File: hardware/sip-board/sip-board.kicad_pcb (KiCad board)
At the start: 8 copper layers, 43 parts, among them IC1 XC7S15-1CPGA196C, J1 Conn_01x06_Pin, J2 Conn_01x10_Pin, J3 Conn_01x10_Pin, J4 Conn_01x10_Pin, J5 Conn_01x10_Pin, SW1 SW_DIP_x03, U1 M95256-WMN6P, U2 TLV75710PDRV, U3 TLV75718PDRV, U4 TLV75733PDRV

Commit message: begin layout for sip
we will need to use pcbway
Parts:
- added C10: 0.47u, Capacitor_SMD:C_0201_0603Metric, F.Cu at (18.9, 62.8)
- added C11: 0.47u, Capacitor_SMD:C_0201_0603Metric, F.Cu at (18.9, 64.6)
- added C12: 47u, Capacitor_SMD:C_0201_0603Metric, F.Cu at (18.9, 66.3)
- added C13: 4.7u, Capacitor_SMD:C_0201_0603Metric, F.Cu at (18.9, 68.1)
- added C14: 0.47u, Capacitor_SMD:C_0201_0603Metric, F.Cu at (21.3, 57.6)
- added C15: 47u, Capacitor_SMD:C_0201_0603Metric, F.Cu at (21.3, 59.3)
- added C16: 4.7u, Capacitor_SMD:C_0201_0603Metric, F.Cu at (21.3, 61.1)
- added C17: 0.47u, Capacitor_SMD:C_0201_0603Metric, F.Cu at (21.3, 62.8)
- added C18: 0.47u, Capacitor_SMD:C_0201_0603Metric, F.Cu at (21.3, 64.6)
- added C19: 0.47u, Capacitor_SMD:C_0201_0603Metric, F.Cu at (21.3, 66.3)
- added C20: 0.47u, Capacitor_SMD:C_0201_0603Metric, F.Cu at (21.3, 68.1)
- added C21: 100u, Capacitor_SMD:C_0201_0603Metric, F.Cu at (23.8, 57.6)
- added C22: 4.7u, Capacitor_SMD:C_0201_0603Metric, F.Cu at (23.8, 59.3)
- added C23: 4.7u, Capacitor_SMD:C_0201_0603Metric, F.Cu at (23.8, 61.1)
- added C24: 0.47u, Capacitor_SMD:C_0201_0603Metric, F.Cu at (23.8, 62.8)
- added C25: 0.47u, Capacitor_SMD:C_0201_0603Metric, F.Cu at (23.8, 64.6)
- added C26: 0.47u, Capacitor_SMD:C_0201_0603Metric, F.Cu at (23.8, 66.3)
- added C27: 0.47u, Capacitor_SMD:C_0201_0603Metric, F.Cu at (23.8, 68.1)
- added C28: 0.47u, Capacitor_SMD:C_0201_0603Metric, F.Cu at (26.2, 57.6)
- added C29: 0.47u, Capacitor_SMD:C_0201_0603Metric, F.Cu at (26.2, 59.3)
- added C30: 100u, Capacitor_SMD:C_0201_0603Metric, F.Cu at (26.2, 61.1)
- added C31: 4.7u, Capacitor_SMD:C_0201_0603Metric, F.Cu at (26.2, 62.8)
- added C32: 4.7u, Capacitor_SMD:C_0201_0603Metric, F.Cu at (26.2, 64.6)
- added C33: 0.47u, Capacitor_SMD:C_0201_0603Metric, F.Cu at (26.2, 66.3)
- added C34: 0.47u, Capacitor_SMD:C_0201_0603Metric, F.Cu at (26.2, 68.1)
- added C35: 0.47u, Capacitor_SMD:C_0201_0603Metric, F.Cu at (28.7, 57.6)
- added C36: 0.47u, Capacitor_SMD:C_0201_0603Metric, F.Cu at (28.7, 59.3)
- added C37: 100u, Capacitor_SMD:C_0201_0603Metric, F.Cu at (28.7, 61.1)
- added C38: 4.7u, Capacitor_SMD:C_0201_0603Metric, F.Cu at (28.7, 62.8)
- added C39: 4.7u, Capacitor_SMD:C_0201_0603Metric, F.Cu at (28.7, 64.6)
- added C7: 100u, Capacitor_SMD:C_0201_0603Metric, F.Cu at (18.9, 57.6)
- added C8: 4.7u, Capacitor_SMD:C_0201_0603Metric, F.Cu at (18.9, 59.3)
- added C9: 4.7u, Capacitor_SMD:C_0201_0603Metric, F.Cu at (18.9, 61.1)
- moved IC1 102.8 mm to (148.9, 90.1)
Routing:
- net +3.3V: track 0.00 -> 15.4 mm, vias 0 -> 11
- net +1V0: track 0.00 -> 11.6 mm, vias 0 -> 11
- net +1V8: track 0.00 -> 4.97 mm, vias 0 -> 4
- net GND: track 0.00 -> 0.71 mm
- added copper zone on F.Cu, net GND
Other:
- board outline added: 20.5 x 21.7 mm
- board text added: "PCBway can do smallest 0.15mm annular width for buried/blind vias"

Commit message: fix some connections, layout
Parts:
- removed J1: Conn_01x06_Pin, Connector_PinHeader_2.54mm:PinHeader_1x06_P2.54mm_Vertical
- removed J2, J3, J4, J5: Conn_01x10_Pin, Connector_PinHeader_2.54mm:PinHeader_1x10_P2.54mm_Vertical
- added C40: 10u, Capacitor_SMD:C_0201_0603Metric, F.Cu at (142.7, 117.9)
- added JTAG: Conn_01x06_Pin, Connector_PinHeader_2.54mm:PinHeader_1x06_P2.54mm_Vertical_SMD_Pin1Right, F.Cu at (146.8, 89.7)
- added R16: 5k, Resistor_SMD:R_0201_0603Metric, F.Cu at (152.7, 110.4)
- added SW2: SW_RESET, Button_Switch_SMD:SW_Push_1P1T_NO_6x6mm_H9.5mm, F.Cu at (147.2, 113.7)
- C10, C11, C16, C17, C18, C19, C20, C21, C22, C23, C24, C25, C26, C27, C28, C29, C30, C31, C32, C33, C34, C35, C36, C37, C38, C39, C7, C8, C9, U1, U5, U6: moved to B.Cu
- moved U5 140.8 mm to (142.5, 93.0), turned to 180 degrees
- moved U6 139.4 mm to (142.5, 96.1), turned to 180 degrees
- moved C7 135.3 mm to (145.8, 104.2), turned to 180 degrees
- moved C8 135.0 mm to (145.8, 105.0), turned to 180 degrees
- moved C10 134.8 mm to (147.0, 104.6), turned to -90 degrees
- moved C11 134.7 mm to (147.0, 106.1), turned to 90 degrees
- moved C9 134.6 mm to (145.8, 105.8), turned to 180 degrees
- moved C15 134.4 mm to (153.8, 81.8), turned to -90 degrees
- moved SW1 133.1 mm to (146.7, 123.4), turned to 90 degrees
- moved C18 132.6 mm to (148.3, 102.6), turned to 90 degrees
- moved C30 132.5 mm to (151.5, 104.0), turned to 90 degrees
- moved C29 131.9 mm to (148.7, 108.3), turned to -90 degrees
- moved C17 131.9 mm to (147.1, 102.3)
- moved C28 131.9 mm to (147.9, 108.3), turned to -90 degrees
- moved C27 131.3 mm to (149.1, 107.2)
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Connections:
- C19 pad 1: +3.3V -> +3V3
- C20 pad 1: +3.3V -> +3V3
- C21 pad 1: +3.3V -> +3V3
- C22 pad 1: +3.3V -> +3V3
- C23 pad 1: +3.3V -> +3V3
- C24 pad 1: +3.3V -> +3V3
- C25 pad 1: +3.3V -> +3V3
- C26 pad 1: +3.3V -> +3V3
- C27 pad 1: +3.3V -> +3V3
- C28 pad 1: +3.3V -> +3V3
- C29 pad 1: +3.3V -> +3V3
- C30 pad 1: +3.3V -> +3V3
- C31 pad 1: +3.3V -> +3V3
- C32 pad 1: +3.3V -> +3V3
- C33 pad 1: +3.3V -> +3V3
- C34 pad 1: +3.3V -> +3V3
- C35 pad 1: +3.3V -> +3V3
- C36 pad 1: +3.3V -> +3V3
- C37 pad 1: +3.3V -> +3V3
- C38 pad 1: +3.3V -> +3V3
- C39 pad 1: +3.3V -> +3V3
- C6 pad 1: +3.3V -> +3V3
- D1 pad 1: +3.3V -> +3V3
- IC1 pad A8: TCK -> CCLK
- IC1 pad E5: +3.3V -> +3V3
- IC1 pad F10: +3.3V -> +3V3
- IC1 pad G5: +3.3V -> +3V3
- IC1 pad H10: +3.3V -> +3V3
- IC1 pad K10: +3.3V -> +3V3
- IC1 pad L7: TMS -> CS
- IC1 pad M7: TDI -> MOSI
- IC1 pad N6: +3.3V -> +3V3
- IC1 pad N9: +3.3V -> +3V3
- IC1 pad P8: +3.3V -> +3V3
- R4 pad 1: +3.3V -> +3V3
- R5 pad 1: +3.3V -> +3V3
- SW1 pad 1: +3.3V -> +3V3
- SW1 pad 2: +3.3V -> +3V3
- SW1 pad 3: +3.3V -> +3V3
- U1 pad 3: +3.3V -> +3V3
- U1 pad 7: +3.3V -> +3V3
- U1 pad 8: +3.3V -> +3V3
- U4 pad 1: +3.3V -> +3V3
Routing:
- net +3V3: track 0.00 -> 63.7 mm, vias 0 -> 21
- net MOSI: track 0.00 -> 40.3 mm, vias 0 -> 3
- net CS: track 0.00 -> 37.0 mm, vias 0 -> 5
- net +1V8: track 4.97 -> 34.9 mm
- net TDO: track 0.00 -> 25.3 mm, vias 0 -> 2
- net GND: track 0.71 -> 21.7 mm, vias 0 -> 78
- net CCLK: track 0.00 -> 17.5 mm, vias 0 -> 2
- net M2_CONFIG: track 0.00 -> 15.5 mm, vias 0 -> 2
- net +3.3V: track 15.4 -> 0.00 mm, vias 11 -> 0
- net DIN: track 0.00 -> 15.0 mm, vias 0 -> 2
- net M0_CONFIG: track 0.00 -> 13.7 mm, vias 0 -> 2
- net M1_CONFIG: track 0.00 -> 13.5 mm, vias 0 -> 2
- net +5V: track 0.00 -> 11.1 mm
- net Net-(C40-Pad1): track 0.00 -> 10.1 mm
- net PROGRAM_B: track 0.00 -> 9.75 mm
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- added copper zone on In3.Cu, net +1V0
- added copper zone on In2.Cu, net +3V3
- added copper zone on B.Cu, net GND
- added copper zone on In1.Cu, net GND
- removed copper zone on F.Cu, net GND
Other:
- board size 20.5 x 21.7 mm -> 20 x 53.1 mm
- board text added: "1V0 LDO"
- board text added: "1V8 LDO"
- board text added: "3V3 LDO"
- board text added: "CCLK"
- board text added: "CS"
- board text added: "M0"
- board text added: "M1"
- board text added: "M2"
- board text added: "MOSI"
- board text added: "Off/On"
- board text added: "RESET"
- board text added: "SPI - [001] JTAG - [101]"
- board text added: "SPI PROM"
- board text added: "TDO"

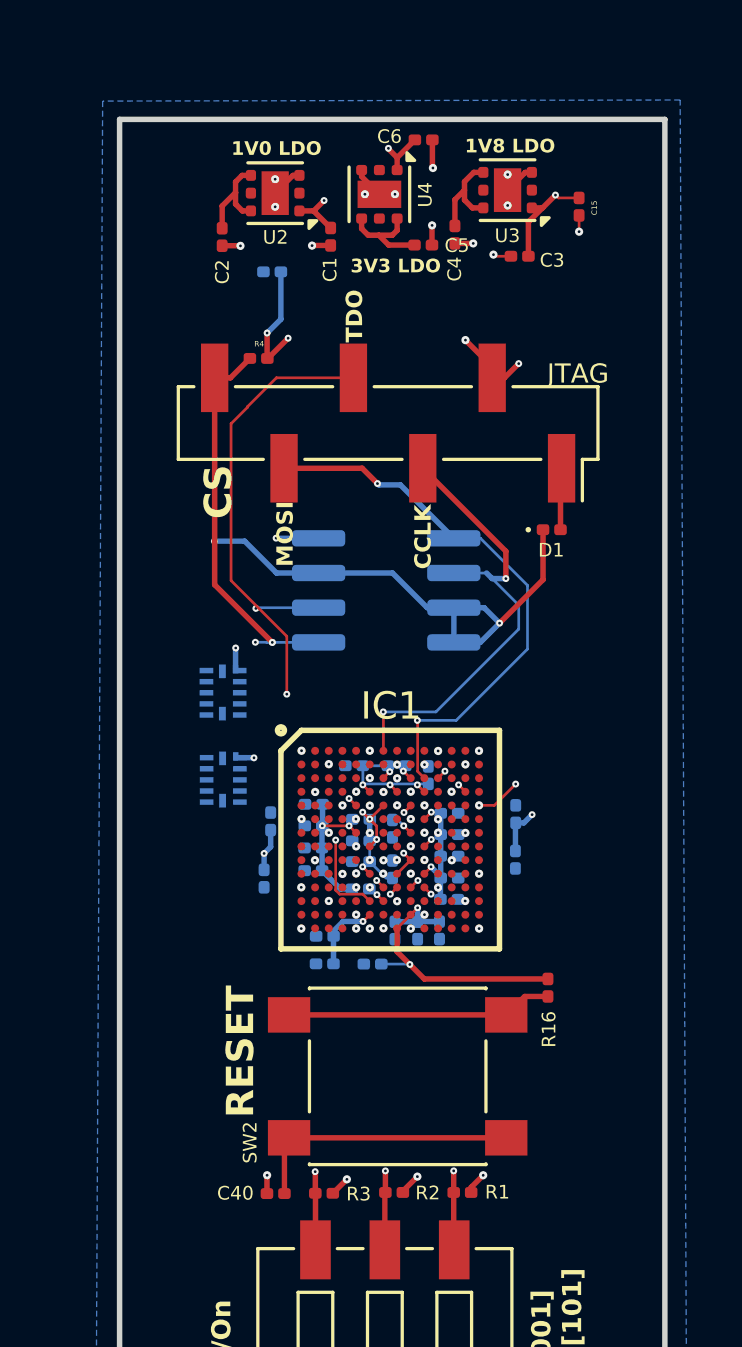
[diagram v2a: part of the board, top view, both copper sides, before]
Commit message: update via settings
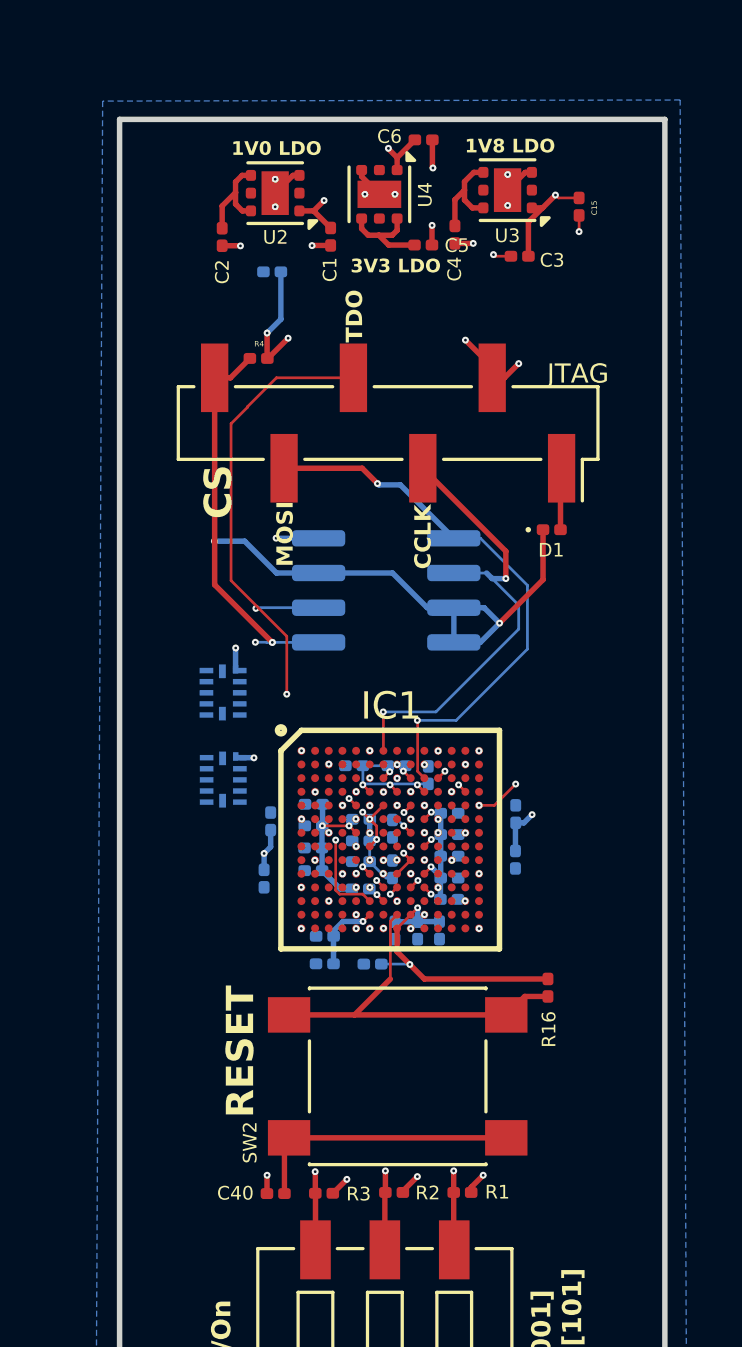
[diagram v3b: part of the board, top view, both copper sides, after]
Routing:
- net PROGRAM_B: track 9.75 -> 16.5 mm

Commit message: redid part of the board
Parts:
- removed C38, C39: 4.7u, Capacitor_SMD:C_0201_0603Metric
- removed C40: 10u, Capacitor_SMD:C_0201_0603Metric
- removed JTAG: Conn_01x06_Pin, Connector_PinHeader_2.54mm:PinHeader_1x06_P2.54mm_Vertical_SMD_Pin1Right
- removed the R16 at (152.7, 110.4)
- removed the R4 at (142.1, 87.4)
- added D2: LED, LED_SMD:LED_0201_0603Metric, F.Cu at (152.2, 103.2)
- added D3: LED, LED_SMD:LED_0201_0603Metric, F.Cu at (140.8, 91.1)
- added D4: LED, LED_SMD:LED_0201_0603Metric, F.Cu at (144.9, 91.2)
- added D5: LED, LED_SMD:LED_0201_0603Metric, F.Cu at (148.7, 91.1)
- added D6: LED, LED_SMD:LED_0201_0603Metric, F.Cu at (141.8, 102.0)
- added J1: Conn_01x06_Pin, Connector_PinHeader_2.54mm:PinHeader_1x06_P2.54mm_Vertical_SMD_Pin1Right, F.Cu at (147.1, 82.6)
- added J2: Conn_01x10_Pin, Connector_PinHeader_2.54mm:PinHeader_1x10_P2.54mm_Vertical, F.Cu at (67.7, 71.1)
- added J3: Conn_01x10_Pin, Connector_PinHeader_2.54mm:PinHeader_1x10_P2.54mm_Vertical, F.Cu at (72.4, 71.1)
- added J4: Conn_01x10_Pin, Connector_PinHeader_2.54mm:PinHeader_1x10_P2.54mm_Vertical, F.Cu at (77.0, 71.1)
- added J5: Conn_01x10_Pin, Connector_PinHeader_2.54mm:PinHeader_1x10_P2.54mm_Vertical, F.Cu at (81.7, 71.1)
- added R14: 5k, Resistor_SMD:R_0201_0603Metric, F.Cu at (147.3, 105.8)
- added R15: 2k4, Resistor_SMD:R_0201_0603Metric, F.Cu at (152.6, 92.4)
- added R17: 5k7, Resistor_SMD:R_0201_0603Metric, F.Cu at (151.8, 104.4)
- added R18: 2k3, Resistor_SMD:R_0201_0603Metric, F.Cu at (141.1, 95.1)
- added R19: 3k, Resistor_SMD:R_0201_0603Metric, F.Cu at (144.9, 94.9)
- added R20: 5k7, Resistor_SMD:R_0201_0603Metric, F.Cu at (148.7, 94.4)
- C1: value 1u -> 10u
- C11: value 0.47u -> 10u; moved to F.Cu
- C12: value 47u -> 0.47u; moved to B.Cu
- C13: value 4.7u -> 0.47u; moved to B.Cu
- C14: value 0.47u -> 100u; moved to B.Cu
- C15: value 47u -> 100u; moved to B.Cu
- C16, U5, U6: moved to F.Cu
- C17, C18, C19, C26, C27, C29, C36: value 0.47u -> 4.7u; moved to F.Cu
- C2: value 10u -> 50u
- C21, C30, C7: value 100u -> 0.47u
- C22, C23, C31, C32, C8, C9: value 4.7u -> 0.47u
- C24: value 0.47u -> 47u
- C25, C35: value 0.47u -> 100u
- C3: value 1u -> 50u
- C37: value 100u -> 4.7u; moved to F.Cu
- C4: value 50u -> 1u
- C5: value 50u -> 100u
- C6: value 100u -> 1u
- U1: value M95256-WMN6P -> TLV75718PDRV; footprint Package_SO:SOIC-8_3.9x4.9mm_P1.27mm -> Package_SON:WSON-6-1EP_2x2mm_P0.65mm_EP1x1.6mm; moved to F.Cu
- U2: value TLV75710PDRV -> TLV75733PDRV
- U3: value TLV75718PDRV -> TLV75710PDRV
- U4: value TLV75733PDRV -> M95256-WMN6P; footprint Package_SON:WSON-6-1EP_2x2mm_P0.65mm_EP1x1.6mm -> Package_SO:SOIC-8_3.9x4.9mm_P1.27mm; moved to B.Cu
- moved C13 134.4 mm to (147.9, 105.8)
- moved C12 134.4 mm to (148.7, 101.1)
- moved C14 127.1 mm to (142.5, 96.1), turned to -90 degrees
- moved R16 110.0 mm to (141.8, 102.8)
- moved U5 67.1 mm to (75.5, 97.0), turned to 0 degrees
- moved U6 63.2 mm to (79.3, 97.0), turned to 0 degrees
- moved C15 22.4 mm to (149.1, 103.7)
- moved C6 16.3 mm to (143.7, 95.1)
- moved U3 14.5 mm to (143.1, 93.3), turned to 90 degrees
- moved U2 14.3 mm to (150.5, 93.3), turned to 90 degrees
- moved D1 13.9 mm to (140.7, 86.9), turned to 90 degrees
- moved C4 12.7 mm to (146.4, 95.2), turned to 0 degrees
- moved C29 12.6 mm to (150.2, 95.8), turned to 0 degrees
- moved C5 12.2 mm to (151.3, 95.0)
- moved C22 11.9 mm to (149.6, 98.8), turned to 0 degrees
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- renumbered R12 to R10, R13 to R11, R14 to R12, R15 to R13, R5 to R16, R6 to R4, R7 to R5, R8 to R6, R9 to R7, R10 to R8, R11 to R9
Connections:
- C1 pad 1: +1V0 -> +5V
- C10 pad 1: +1V0 -> +3V3
- C11 pad 1: +1V0 -> Net-(C11-Pad1)
- C13 pad 1: +1V0 -> +3V3
- C15 pad 1: +1V8 -> +3V3
- C16 pad 1: +1V8 -> +1V0
- C17 pad 1: +1V8 -> +3V3
- C18 pad 1: +1V8 -> +1V0
- C24 pad 1: +3V3 -> +1V8
- C26 pad 1: +3V3 -> +1V8
- C28 pad 1: +3V3 -> +1V8
- C3 pad 1: +1V8 -> +5V
- C30 pad 1: +3V3 -> +1V8
- C4 pad 1: +5V -> +1V8
- C5 pad 1: +5V -> +3V3
- C6 pad 1: +3V3 -> +1V0
- C7 pad 1: +1V0 -> +3V3
- C8 pad 1: +1V0 -> +3V3
- R16 pad 1: +3V3 -> Net-(D6-A)
- SW2 pad 2: Net-(C40-Pad1) -> Net-(C11-Pad1)
- U1 pad 1: CS -> +1V8
- U1 pad 2: DIN -> unconnected-(U1-NC-Pad2)
- U1 pad 3: +3V3 -> GND
- U1 pad 4: GND -> +5V
- U1 pad 5: MOSI -> unconnected-(U1-NC-Pad5)
- U1 pad 6: CCLK -> +5V
- U1 pad 7: +3V3 -> GND
- U2 pad 1: +1V0 -> +3V3
- U3 pad 1: +1V8 -> +1V0
- U4 pad 1: +3V3 -> CS
- U4 pad 2: unconnected-(U4-NC-Pad2) -> DIN
- U4 pad 3: GND -> +3V3
- U4 pad 4: +5V -> GND
- U4 pad 5: unconnected-(U4-NC-Pad5) -> MOSI
- U4 pad 6: +5V -> CCLK
- U4 pad 7: GND -> +3V3
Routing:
- net GND: track 21.7 -> 55.1 mm, vias 78 -> 50
- net MOSI: track 40.3 -> 65.3 mm, vias 3 -> 6
- net +3V3: track 63.7 -> 39.6 mm, vias 21 -> 22
- net +1V8: track 34.9 -> 15.1 mm
- net DIN: track 15.0 -> 0.00 mm, vias 2 -> 0
- net Net-(C40-Pad1): track 10.1 -> 0.00 mm
- net CS: track 37.0 -> 46.4 mm, vias 5 -> 3
- net Net-(C11-Pad1): track 0.00 -> 9.44 mm
- net CCLK: track 17.5 -> 23.3 mm, vias 2 -> 3
- net PROGRAM_B: track 16.5 -> 11.2 mm
- net Net-(IC1-INIT_B_0): track 0.00 -> 5.25 mm, vias 0 -> 2
- net +5V: track 11.1 -> 6.58 mm
- net DONE: track 0.00 -> 4.50 mm, vias 0 -> 2
- net TDO: track 25.3 -> 20.8 mm, vias 2 -> 3
- net Net-(D3-A): track 0.00 -> 3.67 mm
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- added copper zone on In4.Cu, net GND
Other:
- board text added: "1V0"
- board text added: "1V8"
- board text added: "3V3"
- board text added: "VDD GND CCLK TDO MOSI CS"
- board text removed: "1V0 LDO"
- board text removed: "1V8 LDO"
- board text removed: "3V3 LDO"
- board text removed: "CCLK"
- board text removed: "CS"
- board text removed: "MOSI"
- board text removed: "Off/On"
- board text removed: "PCBway can do smallest 0.15mm annular width for buried/blind vias"
- board text removed: "RESET"
- board text removed: "TDO"

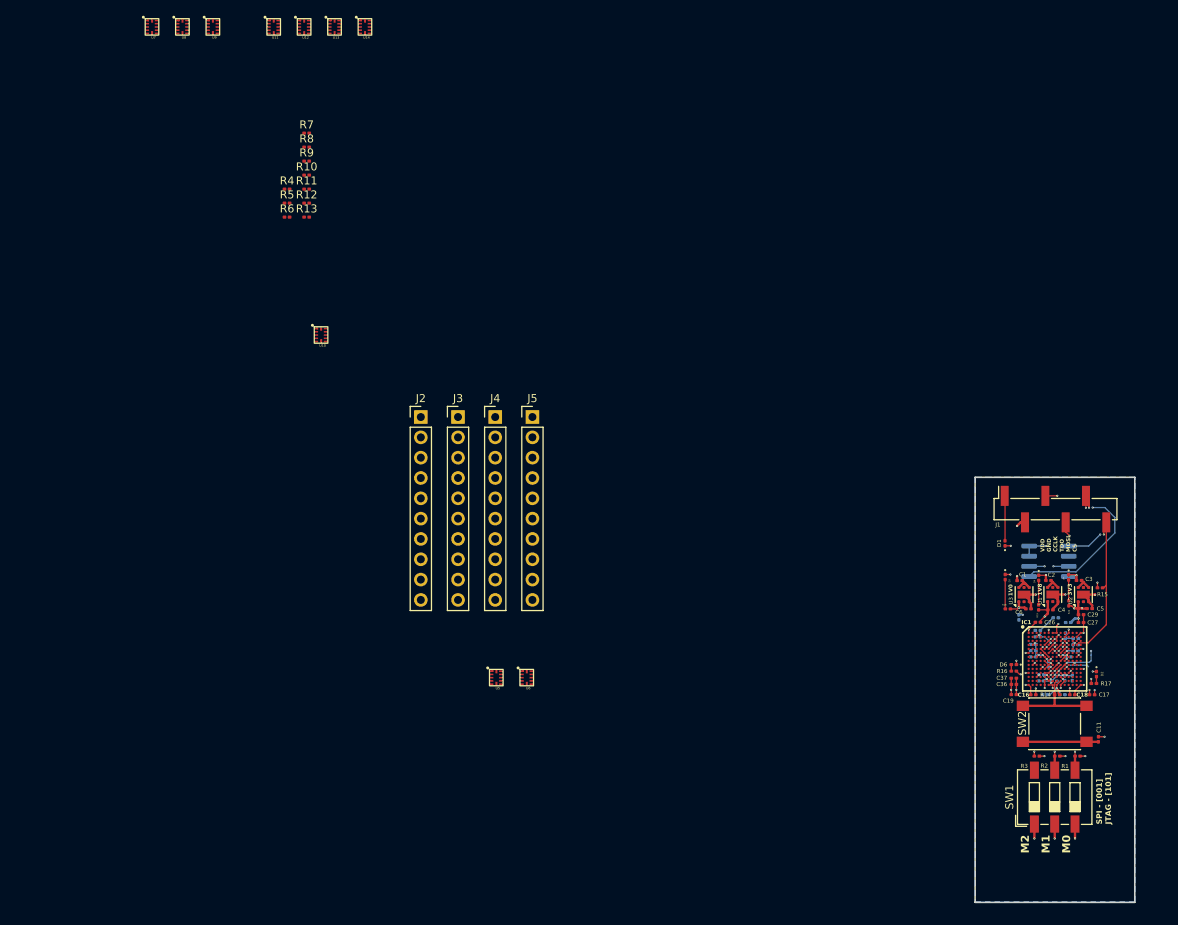
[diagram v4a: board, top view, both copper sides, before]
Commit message: castellated hole edges, add 3d model
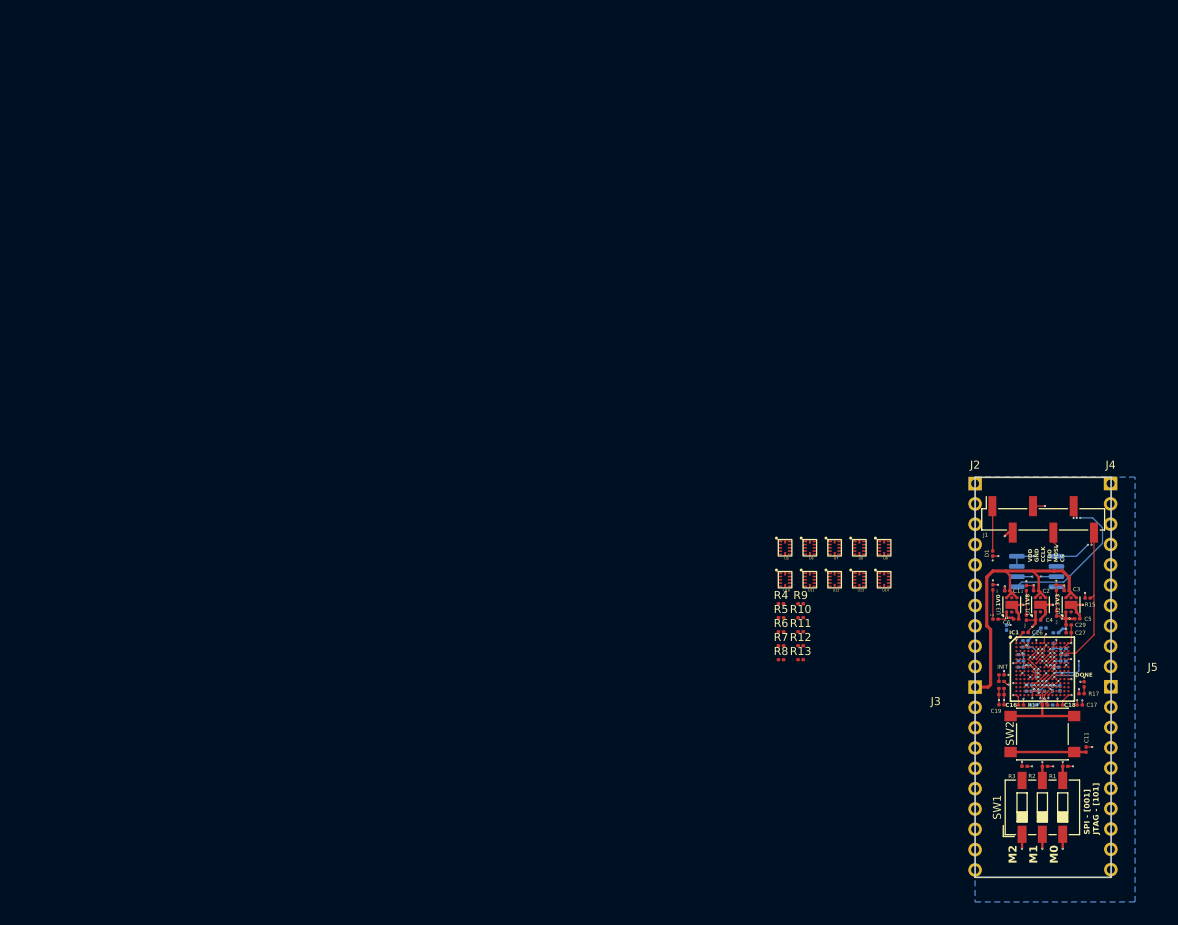
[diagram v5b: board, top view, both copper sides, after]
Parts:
- moved U7 113.8 mm to (119.6, 88.8)
- moved U8 113.3 mm to (122.7, 88.8)
- moved U9 112.7 mm to (125.8, 88.8)
- moved U11 103.4 mm to (116.5, 92.8)
- moved U12 102.9 mm to (119.6, 92.8)
- moved U13 102.5 mm to (122.7, 92.8)
- moved U14 102.0 mm to (125.8, 92.8)
- moved R7 87.3 mm to (112.7, 99.7)
- moved R8 87.3 mm to (112.7, 101.4)
- moved R10 82.9 mm to (115.2, 96.2)
- moved R11 82.9 mm to (115.2, 97.9)
- moved R12 82.9 mm to (115.2, 99.7)
- moved R13 82.9 mm to (115.2, 101.4)
- moved R9 82.9 mm to (115.2, 94.4)
- moved R4 80.6 mm to (112.7, 94.4)
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- renumbered D2 to DONE, D6 to INIT
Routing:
- net +5V: track 6.58 -> 40.4 mm
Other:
- board size 20 x 53.1 mm -> 17 x 50 mm
